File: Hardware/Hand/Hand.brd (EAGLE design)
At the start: 100 x 80 mm, 27 parts, among them T1 2N3904, T2 2N3904, T3 2N3904

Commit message: Hand PCB Rev0 complete.
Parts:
- removed C6: 1uF, rcl:C025-025X050
- removed G1: AB9V, battery:AB9V
- removed LEDU1RX, LEDU1TX, LEDXBON: (no value), led:LED5MM
- removed R1, R10, R11, R12, R13, R15, R16, R17, R2, R3, R4, R5, R6, R7, R8, R9: (no value), rcl:0207/7
- added BAT9V, TIVA5V: (no value), pinhead:1X02
- added C1, C2, C3, C4: (no value), rcl:C025-025X050
- added FLEX0, FLEX1, FLEX2, FLEX3, FLEX4: (no value), con-lstb:MA03-1
- added LED0, LED1, LED2, LED3, LED4, LEDON, LEDRSSI, LEDRX, LEDTX: (no value), led:LED5MM
- added R-B0, R-B1, R-B2, R-B3, R-B4, R-BON, R-BRSSI, R-BRX, R-BTX, R-C0, R-C1, R-C2, R-C3, R-C4, R-CON, R-CRSSI, R-CRX, R-CTX, R-VD0, R-VD1, R-VD2, R-VD3, R-VD4: (no value), resistor:0204/7
- added REG3V3, REG5V: 7805TV, linear:TO220V
- added T0, T4, TON, TRSSI, TRX, TTX: 2N3904, transistor:TO92
- C5: value 8.2pF -> (none)
- moved XB1 174.1 mm to (92.1, 41.9)
- moved C5 155.8 mm to (73.7, 49.5), turned to 270 degrees
- moved T3 146.7 mm to (18.4, 19.1), turned to 270 degrees
- moved T2 129.4 mm to (18.4, 29.2), turned to 270 degrees
- moved T1 112.2 mm to (18.4, 39.4), turned to 270 degrees
- moved TIVA1 87.9 mm to (45.7, 27.9), turned to 90 degrees
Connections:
- removed net 3.3V: TIVA1.3.3V
- removed net B$1: R10.2, R11.2, R12.2, R13.2, R4.2, R5.2, R6.2, R7.2, R8.2, R9.2, TIVA1.PF0, TIVA1.PF1, TIVA1.PF2, TIVA1.PF3, TIVA1.PF4
- removed net GPIOE1: TIVA1.PE1, XB1.6
- removed net GPIOE2: TIVA1.PE2, XB1.12
- removed net GPIOE3: TIVA1.PE3, XB1.16
- removed net U1RX: R15.2, TIVA1.PB0, XB1.2
- removed net U1TX: R16.2, TIVA1.PB1, XB1.3
- removed net XBON: R17.2, XB1.13
- new net 9V: BAT9V.2, C1.1, REG5V.1
- new net N$10: R-B1.2, T1.2
- new net N$11: LED4.K, R-C4.2
- new net N$12: LED2.K, R-C2.2
- new net N$13: FLEX2.2, FLEX2.3, R-B2.1, R-VD2.2, TIVA1.PD2
- new net N$14: R-B2.2, T2.2
- new net N$15: R-C0.1, T0.1
- new net N$16: LED0.K, R-C0.2
- new net N$17: FLEX3.2, FLEX3.3, R-B3.1, R-VD3.2, TIVA1.PD1
- new net N$18: R-B3.2, T3.2
- new net N$19: R-BTX.1, TIVA1.PC7, XB1.3
- new net N$20: R-BRX.1, TIVA1.PC6, XB1.2
- new net N$21: FLEX4.2, FLEX4.3, R-B4.1, R-VD4.2, TIVA1.PD0
- new net N$22: R-B4.2, T4.2
- new net N$23: R-BTX.2, TTX.2
- new net N$24: R-CTX.1, TTX.1
- new net N$25: LEDTX.K, R-CTX.2
- new net N$26: R-BRX.2, TRX.2
- new net N$27: R-CRX.1, TRX.1
- new net N$31: R-BRSSI.2, TRSSI.2
- new net N$32: R-CRSSI.1, TRSSI.1
- new net N$33: LEDRSSI.K, R-CRSSI.2
- new net N$34: R-BON.2, TON.2
- new net N$35: R-CON.1, TON.1
- new net N$36: LEDON.K, R-CON.2
- new net N$7: LED3.K, R-C3.2
- new net N$8: R-C4.1, T4.1
- new net N$9: FLEX1.2, FLEX1.3, R-B1.1, R-VD1.2, TIVA1.PD3
- net 3V3: now also C3.1, C4.1, LED0.A, LED1.A, LED2.A, LED3.A, LED4.A, LEDON.A, LEDRSSI.A, LEDRX.A, LEDTX.A, R-VD0.1, R-VD1.1, R-VD2.1, R-VD3.1, R-VD4.1, REG3V3.3; no longer C6.1
- net 5V: now also C2.1, REG3V3.1, REG5V.3, TIVA5V.2; no longer R1.2, R10.1, R12.1, R2.2, R3.2, R4.1, R6.1, R8.1, TIVA1.5V
- net GND: now also BAT9V.1, C1.2, C2.2, C3.2, C4.2, FLEX0.1, FLEX1.1, FLEX2.1, FLEX3.1, FLEX4.1, REG3V3.2, REG5V.2, T0.3, T4.3, TIVA5V.1, TON.3, TRSSI.3, TRX.3, TTX.3; no longer C6.2, G1.-, R11.1, R13.1, R5.1, R7.1, R9.1
- net N$1: now also FLEX0.2, FLEX0.3, R-B0.1, R-VD0.2, TIVA1.PE1; no longer LEDXBON.K, T1.1
- net N$2: now also R-C1.1, T1.1; no longer LEDU1TX.K, T2.1
- net N$28: now also LEDRX.K, R-CRX.2; no longer R15.1, T3.2
- net N$29: now also R-BRSSI.1, XB1.6; no longer R16.1, T2.2
- net N$3: now also LED1.K, R-C1.2; no longer LEDU1TX.A, R2.1
- net N$30: now also R-BON.1, XB1.13; no longer R17.1, T1.2
- net N$4: now also R-C2.1, T2.1; no longer LEDXBON.A, R1.1
- net N$5: now also R-B0.2, T0.2; no longer LEDU1RX.K, T3.1
- net N$6: now also R-C3.1, T3.1; no longer LEDU1RX.A, R3.1
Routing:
- net 3V3: track 0.00 -> 332.9 mm
- net N$1: track 0.00 -> 102.9 mm
- net N$9: track 0.00 -> 90.2 mm
- net N$13: track 0.00 -> 77.5 mm
- net N$20: track 0.00 -> 74.5 mm
- net N$30: track 0.00 -> 70.0 mm
- net N$17: track 0.00 -> 67.3 mm
- net N$19: track 0.00 -> 62.4 mm
- net N$21: track 0.00 -> 52.1 mm
- net 5V: track 0.00 -> 27.9 mm
- net N$27: track 0.00 -> 17.8 mm
- net N$29: track 0.00 -> 14.0 mm
- net N$24: track 0.00 -> 12.7 mm
- net N$26: track 0.00 -> 8.89 mm
- net N$35: track 0.00 -> 7.62 mm
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- added copper zone on layer 16, net GND
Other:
- board size 100 x 80 mm -> 106.7 x 55.9 mm

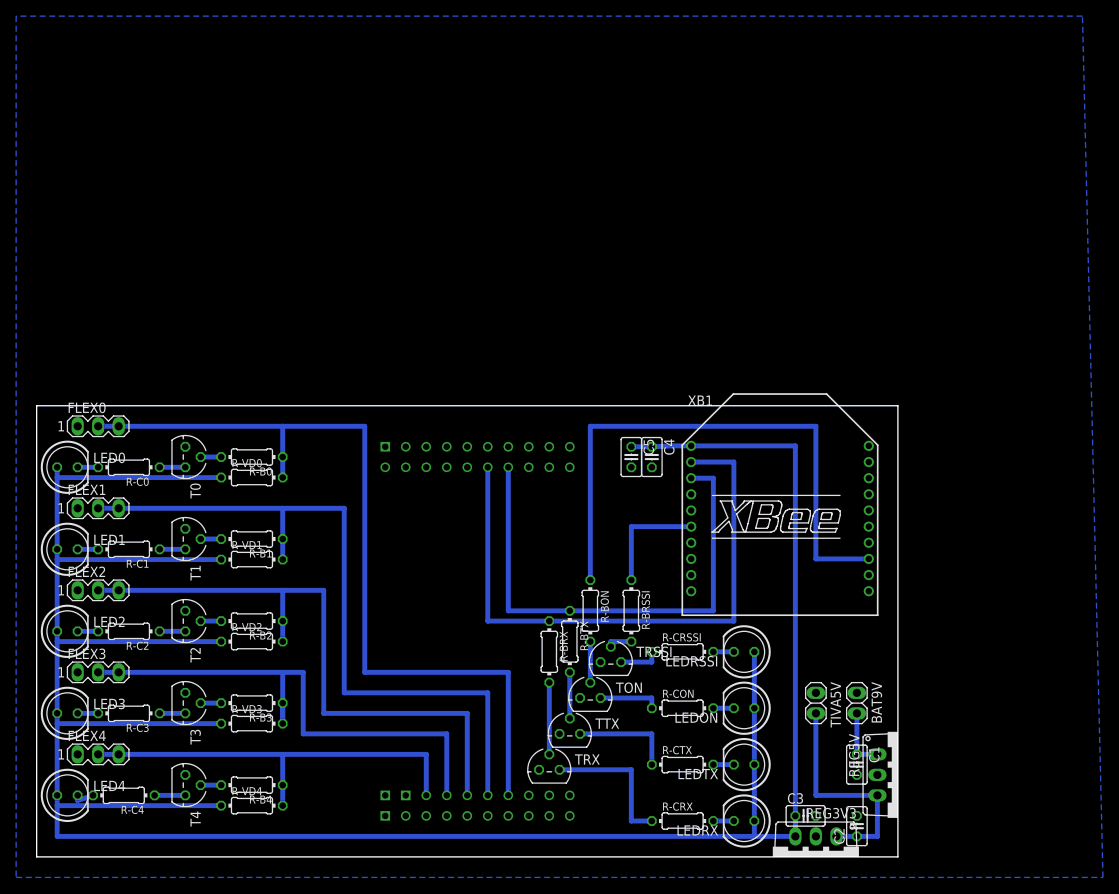
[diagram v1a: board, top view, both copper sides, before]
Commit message: Adjust positions for milling.
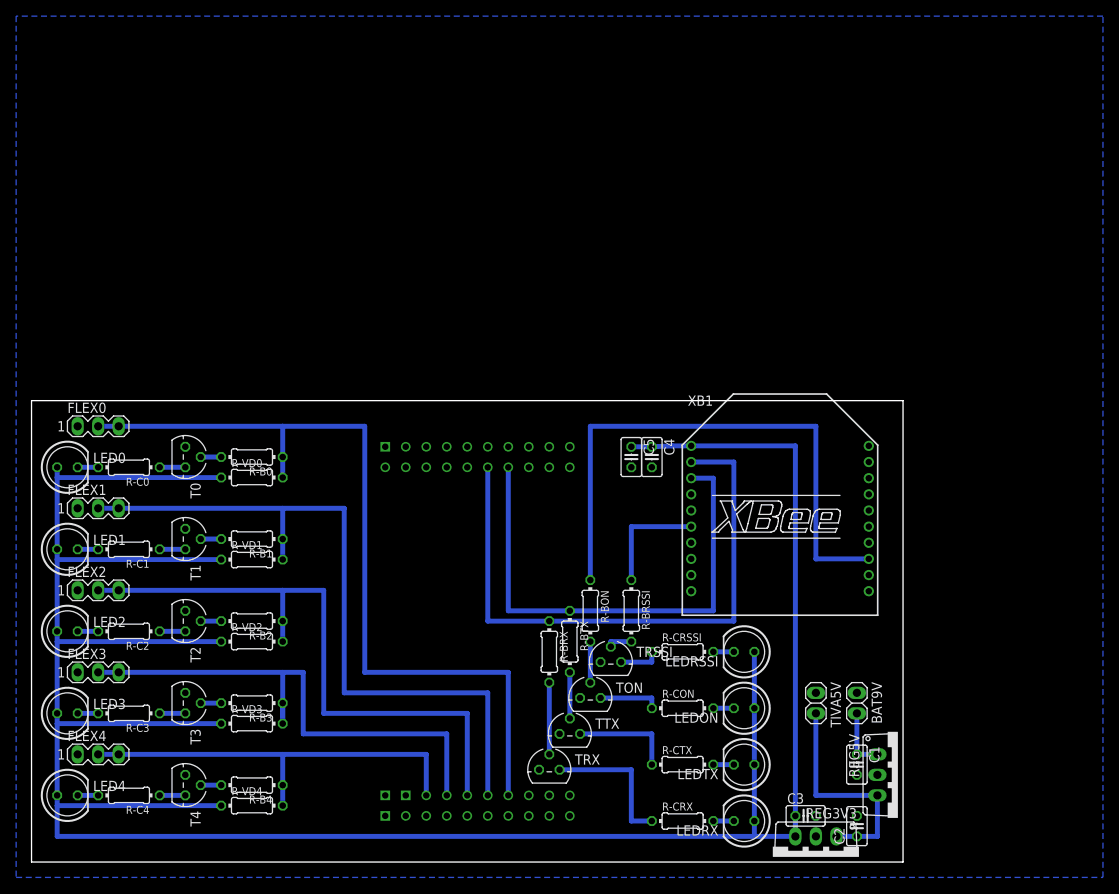
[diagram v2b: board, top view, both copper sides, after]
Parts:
- moved R-C4 0.63 mm to (11.4, 7.62)
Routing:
- net N$8: track 3.81 -> 3.17 mm
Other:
- board size 106.7 x 55.9 mm -> 108 x 57.1 mm
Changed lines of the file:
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@@
 <board>
 <plain>
-<wire x1="0" y1="0" x2="106.68" y2="0" width="0" layer="20"/>
-<wire x1="106.68" y1="0" x2="106.68" y2="55.88" width="0" layer="20"/>
-<wire x1="106.68" y1="55.88" x2="0" y2="55.88" width="0" layer="20"/>
-<wire x1="0" y1="55.88" x2="0" y2="0" width="0" layer="20"/>
+<wire x1="-0.635" y1="-0.635" x2="107.315" y2="-0.635" width="0" layer="20"/>
+<wire x1="107.315" y1="-0.635" x2="107.315" y2="56.515" width="0" layer="20"/>
+<wire x1="107.315" y1="56.515" x2="-0.635" y2="56.515" width="0" layer="20"/>
+<wire x1="-0.635" y1="56.515" x2="-0.635" y2="-0.635" width="0" layer="20"/>
 </plain>
 <attributes>
@@
 <element name="R-C2" library="resistor" package="0204/7" value="" x="11.43" y="27.94" rot="R180"/>
 <element name="R-C3" library="resistor" package="0204/7" value="" x="11.43" y="17.78" rot="R180"/>
-<element name="R-C4" library="resistor" package="0204/7" value="" x="10.795" y="7.62" rot="R180"/>
+<element name="R-C4" library="resistor" package="0204/7" value="" x="11.43" y="7.62" rot="R180"/>
 <element name="R-VD0" library="resistor" package="0204/7" value="" x="26.67" y="46.99"/>
 <element name="R-VD1" library="resistor" package="0204/7" value="" x="26.67" y="36.83"/>
@@
 <contactref element="FLEX4" pad="1"/>
 <contactref element="T4" pad="3"/>
-<polygon width="0.4064" layer="16" isolate="0.6096">
+<polygon width="0.4064" layer="16" isolate="0.508">
 <vertex x="-2.54" y="-2.54"/>
 <vertex x="132.08" y="-2.54"/>
-<vertex x="129.54" y="104.14"/>
+<vertex x="132.08" y="104.14"/>
 <vertex x="-2.54" y="104.14"/>
 </polygon>
@@
 <contactref element="T4" pad="1"/>
 <contactref element="R-C4" pad="1"/>
-<wire x1="14.605" y1="7.62" x2="18.415" y2="7.62" width="0.6096" layer="16"/>
+<wire x1="15.24" y1="7.62" x2="18.415" y2="7.62" width="0.6096" layer="16"/>
 </signal>
 <signal name="N$11">
 <contactref element="R-C4" pad="2"/>
 <contactref element="LED4" pad="K"/>
-<wire x1="5.08" y1="7.62" x2="5.08" y2="6.985" width="0.6096" layer="16"/>
-<wire x1="5.08" y1="6.985" x2="6.985" y2="7.62" width="0.6096" layer="16"/>
+<wire x1="5.08" y1="7.62" x2="7.62" y2="7.62" width="0.6096" layer="16"/>
 </signal>
 <signal name="N$2">
